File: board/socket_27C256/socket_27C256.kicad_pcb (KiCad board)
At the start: 2 copper layers, 17.8 x 35.6 mm, 2 parts, among them J1 Adapter

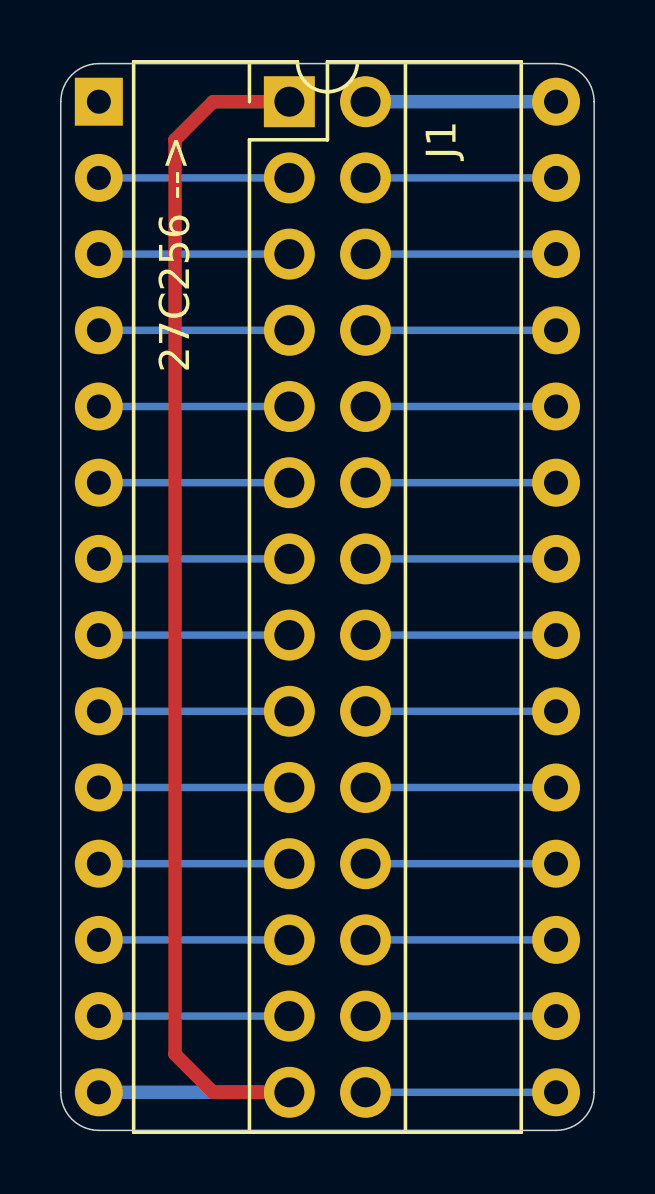
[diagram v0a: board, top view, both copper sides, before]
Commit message: Add 27C400/16 socket
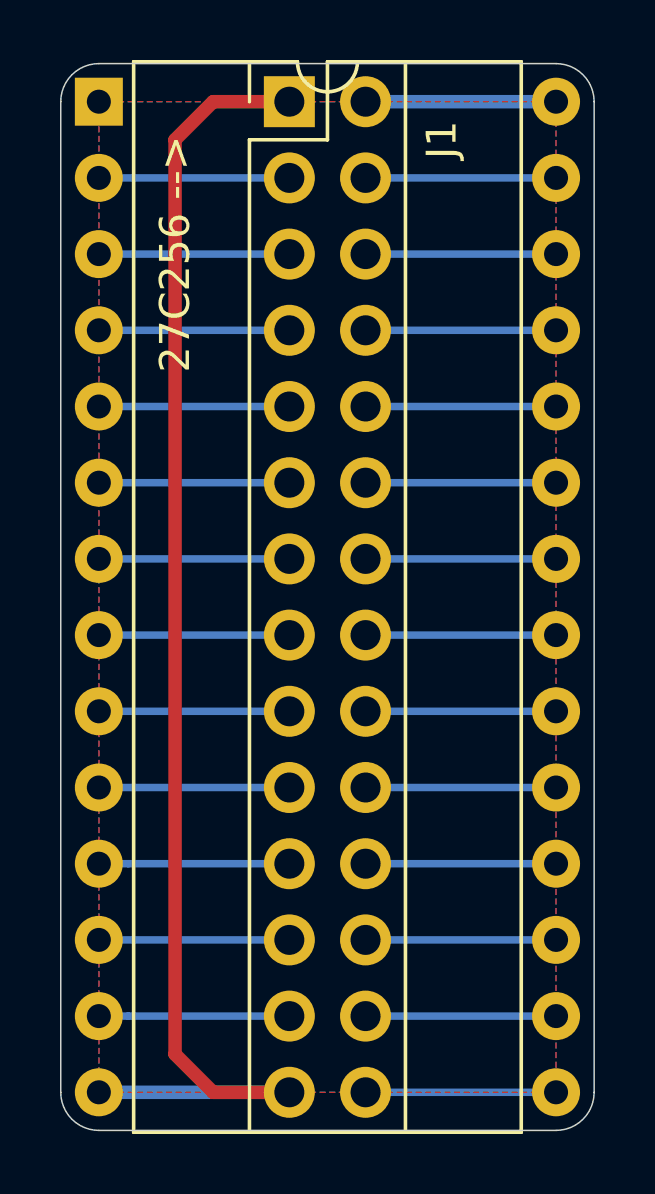
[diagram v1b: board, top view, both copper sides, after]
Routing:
- added copper zone on B.Cu, net GND
- added copper zone on F.Cu, net GND
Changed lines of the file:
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@@
     (add_net /~CE)
     (add_net /~OE)
-    (add_net "Net-(U1-Pad1)")
   )
   (net_class POWER ""
@@
       (effects (font (size 1 1) (thickness 0.15)))
     )
+    (fp_line (start 16.3 -1.55) (end -1.05 -1.55) (layer F.CrtYd) (width 0.05))
+    (fp_line (start 16.3 34.55) (end 16.3 -1.55) (layer F.CrtYd) (width 0.05))
+    (fp_line (start -1.05 34.55) (end 16.3 34.55) (layer F.CrtYd) (width 0.05))
+    (fp_line (start -1.05 -1.55) (end -1.05 34.55) (layer F.CrtYd) (width 0.05))
+    (fp_line (start 14.08 -1.33) (end 8.62 -1.33) (layer F.SilkS) (width 0.12))
+    (fp_line (start 14.08 34.35) (end 14.08 -1.33) (layer F.SilkS) (width 0.12))
+    (fp_line (start 1.16 34.35) (end 14.08 34.35) (layer F.SilkS) (width 0.12))
+    (fp_line (start 1.16 -1.33) (end 1.16 34.35) (layer F.SilkS) (width 0.12))
+    (fp_line (start 6.62 -1.33) (end 1.16 -1.33) (layer F.SilkS) (width 0.12))
+    (fp_line (start 0.255 -0.27) (end 1.255 -1.27) (layer F.Fab) (width 0.1))
+    (fp_line (start 0.255 34.29) (end 0.255 -0.27) (layer F.Fab) (width 0.1))
+    (fp_line (start 14.985 34.29) (end 0.255 34.29) (layer F.Fab) (width 0.1))
+    (fp_line (start 14.985 -1.27) (end 14.985 34.29) (layer F.Fab) (width 0.1))
+    (fp_line (start 1.255 -1.27) (end 14.985 -1.27) (layer F.Fab) (width 0.1))
     (fp_text user %R (at 7.62 16.51) (layer F.Fab)
       (effects (font (size 1 1) (thickness 0.15)))
     )
     (fp_arc (start 7.62 -1.33) (end 6.62 -1.33) (angle -180) (layer F.SilkS) (width 0.12))
-    (fp_line (start 1.255 -1.27) (end 14.985 -1.27) (layer F.Fab) (width 0.1))
-    (fp_line (start 14.985 -1.27) (end 14.985 34.29) (layer F.Fab) (width 0.1))
-    (fp_line (start 14.985 34.29) (end 0.255 34.29) (layer F.Fab) (width 0.1))
-    (fp_line (start 0.255 34.29) (end 0.255 -0.27) (layer F.Fab) (width 0.1))
-    (fp_line (start 0.255 -0.27) (end 1.255 -1.27) (layer F.Fab) (width 0.1))
-    (fp_line (start 6.62 -1.33) (end 1.16 -1.33) (layer F.SilkS) (width 0.12))
-    (fp_line (start 1.16 -1.33) (end 1.16 34.35) (layer F.SilkS) (width 0.12))
-    (fp_line (start 1.16 34.35) (end 14.08 34.35) (layer F.SilkS) (width 0.12))
-    (fp_line (start 14.08 34.35) (end 14.08 -1.33) (layer F.SilkS) (width 0.12))
-    (fp_line (start 14.08 -1.33) (end 8.62 -1.33) (layer F.SilkS) (width 0.12))
-    (fp_line (start -1.05 -1.55) (end -1.05 34.55) (layer F.CrtYd) (width 0.05))
-    (fp_line (start -1.05 34.55) (end 16.3 34.55) (layer F.CrtYd) (width 0.05))
-    (fp_line (start 16.3 34.55) (end 16.3 -1.55) (layer F.CrtYd) (width 0.05))
-    (fp_line (start 16.3 -1.55) (end -1.05 -1.55) (layer F.CrtYd) (width 0.05))
     (pad 28 thru_hole oval (at 15.24 0) (size 1.6 1.6) (drill 0.8) (layers *.Cu *.Mask)
       (net 27 /VCC_EXT))
@@
       (effects (font (size 1 1) (thickness 0.15)))
     )
+    (fp_line (start 0 -1.27) (end 3.81 -1.27) (layer F.Fab) (width 0.1))
+    (fp_line (start 3.81 -1.27) (end 3.81 34.29) (layer F.Fab) (width 0.1))
+    (fp_line (start 3.81 34.29) (end -1.27 34.29) (layer F.Fab) (width 0.1))
+    (fp_line (start -1.27 34.29) (end -1.27 0) (layer F.Fab) (width 0.1))
+    (fp_line (start -1.27 0) (end 0 -1.27) (layer F.Fab) (width 0.1))
+    (fp_line (start -1.33 34.35) (end 3.87 34.35) (layer F.SilkS) (width 0.12))
+    (fp_line (start -1.33 1.27) (end -1.33 34.35) (layer F.SilkS) (width 0.12))
+    (fp_line (start 3.87 -1.33) (end 3.87 34.35) (layer F.SilkS) (width 0.12))
+    (fp_line (start -1.33 1.27) (end 1.27 1.27) (layer F.SilkS) (width 0.12))
+    (fp_line (start 1.27 1.27) (end 1.27 -1.33) (layer F.SilkS) (width 0.12))
+    (fp_line (start 1.27 -1.33) (end 3.87 -1.33) (layer F.SilkS) (width 0.12))
+    (fp_line (start -1.33 0) (end -1.33 -1.33) (layer F.SilkS) (width 0.12))
+    (fp_line (start -1.33 -1.33) (end 0 -1.33) (layer F.SilkS) (width 0.12))
+    (fp_line (start -1.8 -1.8) (end -1.8 34.8) (layer F.CrtYd) (width 0.05))
+    (fp_line (start -1.8 34.8) (end 4.35 34.8) (layer F.CrtYd) (width 0.05))
+    (fp_line (start 4.35 34.8) (end 4.35 -1.8) (layer F.CrtYd) (width 0.05))
     (fp_line (start 4.35 -1.8) (end -1.8 -1.8) (layer F.CrtYd) (width 0.05))
-    (fp_line (start 4.35 34.8) (end 4.35 -1.8) (layer F.CrtYd) (width 0.05))
-    (fp_line (start -1.8 34.8) (end 4.35 34.8) (layer F.CrtYd) (width 0.05))
-    (fp_line (start -1.8 -1.8) (end -1.8 34.8) (layer F.CrtYd) (width 0.05))
-    (fp_line (start -1.33 -1.33) (end 0 -1.33) (layer F.SilkS) (width 0.12))
-    (fp_line (start -1.33 0) (end -1.33 -1.33) (layer F.SilkS) (width 0.12))
-    (fp_line (start 1.27 -1.33) (end 3.87 -1.33) (layer F.SilkS) (width 0.12))
-    (fp_line (start 1.27 1.27) (end 1.27 -1.33) (layer F.SilkS) (width 0.12))
-    (fp_line (start -1.33 1.27) (end 1.27 1.27) (layer F.SilkS) (width 0.12))
-    (fp_line (start 3.87 -1.33) (end 3.87 34.35) (layer F.SilkS) (width 0.12))
-    (fp_line (start -1.33 1.27) (end -1.33 34.35) (layer F.SilkS) (width 0.12))
-    (fp_line (start -1.33 34.35) (end 3.87 34.35) (layer F.SilkS) (width 0.12))
-    (fp_line (start -1.27 0) (end 0 -1.27) (layer F.Fab) (width 0.1))
-    (fp_line (start -1.27 34.29) (end -1.27 0) (layer F.Fab) (width 0.1))
-    (fp_line (start 3.81 34.29) (end -1.27 34.29) (layer F.Fab) (width 0.1))
-    (fp_line (start 3.81 -1.27) (end 3.81 34.29) (layer F.Fab) (width 0.1))
-    (fp_line (start 0 -1.27) (end 3.81 -1.27) (layer F.Fab) (width 0.1))
     (fp_text user %R (at 1.27 16.51 90) (layer F.Fab)
       (effects (font (size 1 1) (thickness 0.15)))
@@
   (segment (start 125.73 93.98) (end 119.48 93.98) (width 0.25) (layer B.Cu) (net 12))
   (segment (start 128.27 91.44) (end 134.72 91.44) (width 0.25) (layer B.Cu) (net 13))
+  (segment (start 125.73 91.44) (end 119.48 91.44) (width 0.25) (layer B.Cu) (net 14))
   (segment (start 134.72 88.9) (end 128.27 88.9) (width 0.25) (layer B.Cu) (net 15))
   (segment (start 125.73 88.9) (end 119.48 88.9) (width 0.25) (layer B.Cu) (net 16))
@@
   (segment (start 125.73 76.2) (end 119.48 76.2) (width 0.25) (layer B.Cu) (net 26))
   (segment (start 134.72 73.66) (end 128.27 73.66) (width 0.45) (layer B.Cu) (net 27))
-  (segment (start 125.73 91.44) (end 119.48 91.44) (width 0.25) (layer B.Cu) (net 14))
+  (zone (net 2) (net_name GND) (layer B.Cu) (hatch edge 0.508)
+    (connect_pads (clearance 0.508))
+    (min_thickness 0.254)
+    (fill yes (arc_segments 32) (thermal_gap 0.508) (thermal_bridge_width 0.508))
+    (polygon
+      (pts
+        (xy 134.62 106.68) (xy 119.38 106.68) (xy 119.38 73.66) (xy 134.62 73.66)
+      )
+    )
+  )
+  (zone (net 2) (net_name GND) (layer F.Cu) (hatch edge 0.508)
+    (connect_pads (clearance 0.508))
+    (min_thickness 0.254)
+    (fill yes (arc_segments 32) (thermal_gap 0.508) (thermal_bridge_width 0.508))
+    (polygon
+      (pts
+        (xy 134.62 106.68) (xy 119.38 106.68) (xy 119.38 73.66) (xy 134.62 73.66)
+      )
+    )
+  )
 )
